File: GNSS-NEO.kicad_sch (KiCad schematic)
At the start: 25 parts, among them J3 Conn_Coaxial, J4 Conn_Coaxial_Small, SW1 SW_Push, U2 NEO-M9N

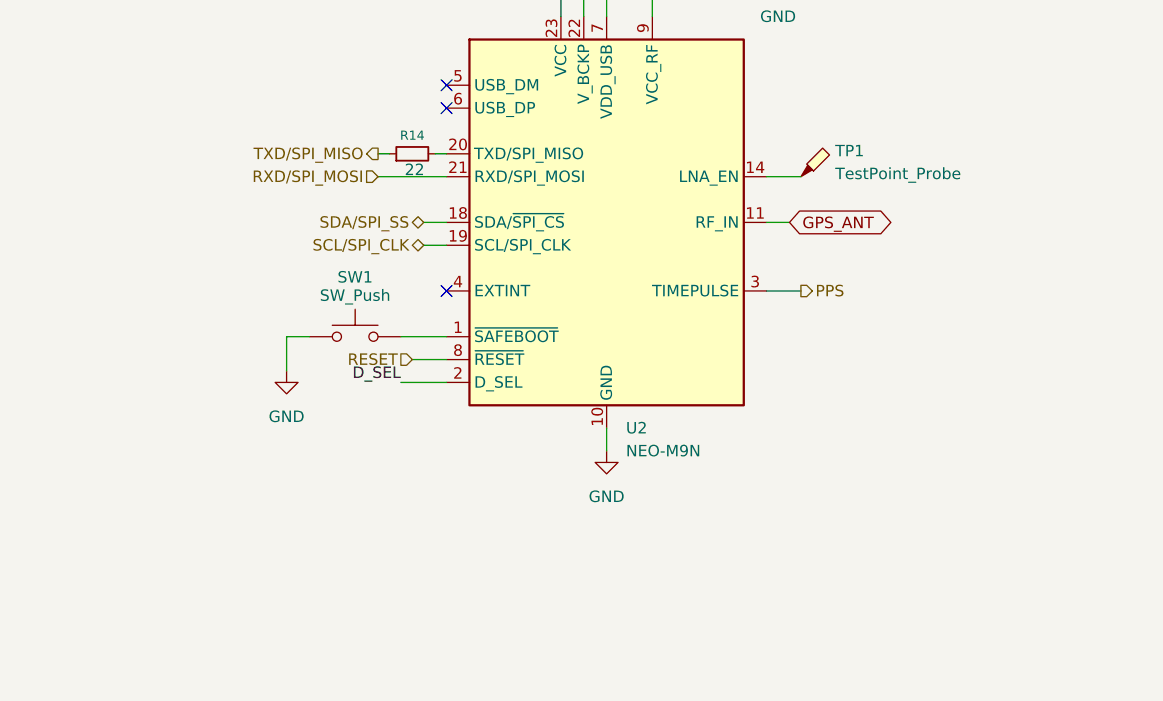
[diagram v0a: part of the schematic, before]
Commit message: Update schematics and rework NEO-M9N reader sketches
Co-Authored-By: Claude Opus 4.8 <noreply@anthropic.com>
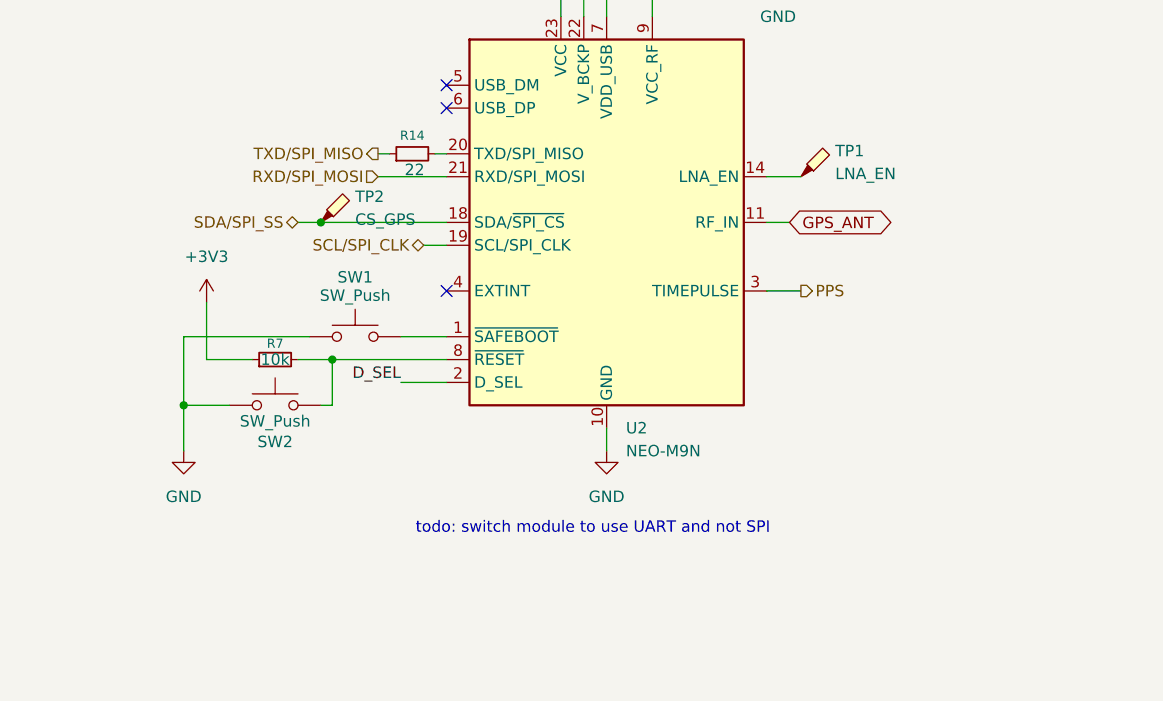
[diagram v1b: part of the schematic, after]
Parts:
- added R7: 10k, Resistor_SMD:R_0402_1005Metric, symbol Device:R_Small
- added SW2: SW_Push, Button_Switch_SMD:SW_Push_SPST_NO_Alps_SKRK, symbol Switch:SW_Push
- added TP2: CS_GPS, TestPoint:TestPoint_Loop_D1.80mm_Drill1.0mm_Beaded, symbol Connector:TestPoint_Probe
- TP1: value TestPoint_Probe -> LNA_EN
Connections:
- net +3V3: now also R7.1
- net GND: now also SW2.1
- net SDA/SPI_SS: now also TP2.1
- net RESET: no longer names the net of U2.8 (~{RESET})
- net RESET: now also R7.2, SW2.2
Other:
- note added: "todo: switch module to use UART and not SPI"
